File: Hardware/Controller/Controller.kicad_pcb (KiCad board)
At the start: 2 copper layers, 33 x 123.2 mm, 6 parts

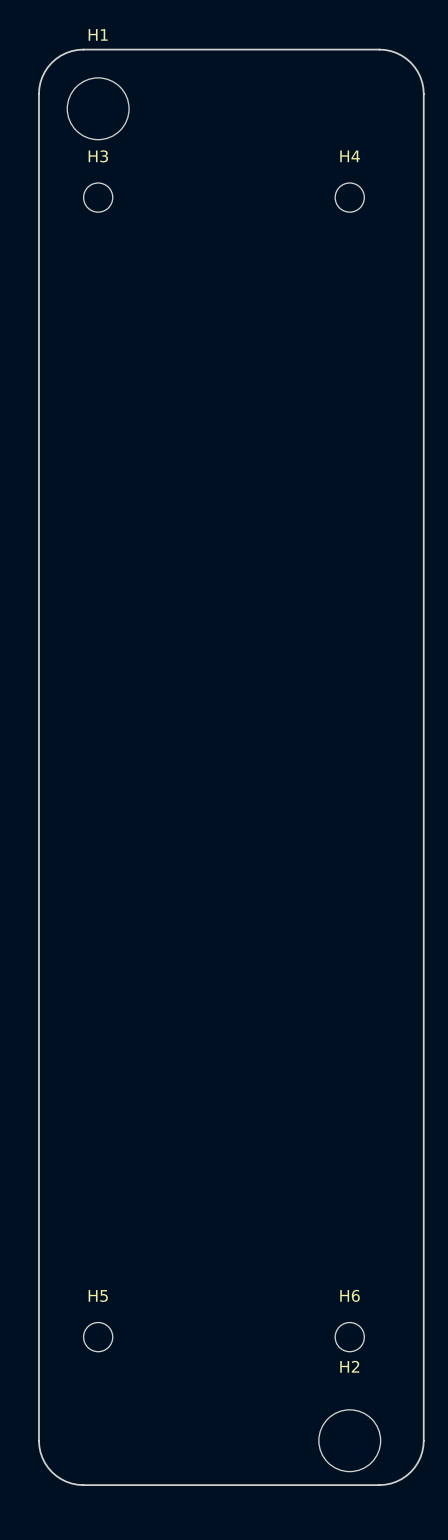
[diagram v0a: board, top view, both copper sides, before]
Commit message: Updated fitting for SP 2090 enclosure
Better fit, but still not perfect.
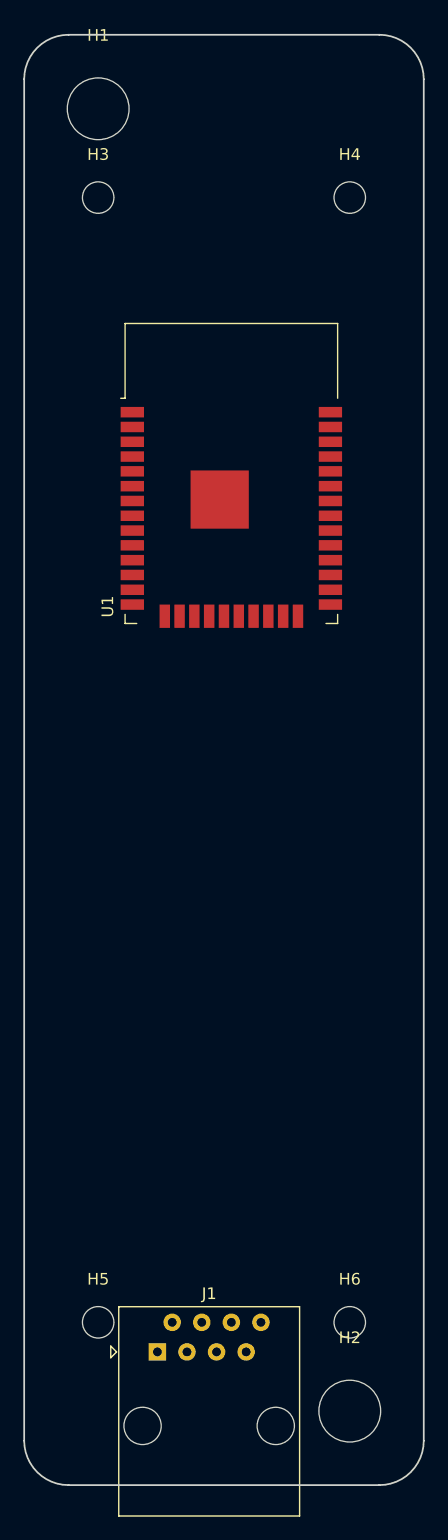
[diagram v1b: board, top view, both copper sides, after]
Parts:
- added J1: 8P8C, Connector_RJ:RJ45_Amphenol_54602-x08_Horizontal, F.Cu at (25.4, 127.0)
- added U1: ESP32-WROOM-32D, RF_Module:ESP32-WROOM-32, F.Cu at (31.8, 54.6)
- H3, H4, H5, H6: footprint MountingHole:MountingHole_2.5mm -> MountingHole:MountingHole_2.7mm_M2.5
- moved H2 2.54 mm to (41.9, 132.1)
- moved H5 1.27 mm to (20.3, 124.5)
- moved H6 1.27 mm to (41.9, 124.5)
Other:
- board size 33 x 123.2 mm -> 34.3 x 124.5 mm

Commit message: Finished case-specific layout parts
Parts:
- moved J1 109.8 mm to (133.5, 108.0)
- moved U1 107.9 mm to (136.8, 79.6)
- moved H3 0.80 mm to (20.8, 27.3)
- moved H4 0.70 mm to (42.2, 27.3)
- moved H5 0.54 mm to (20.8, 124.7)
- moved H1 0.48 mm to (20.8, 20.3)
- moved H2 0.48 mm to (42.2, 131.7)
- moved H6 0.38 mm to (42.2, 124.7)
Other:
- board size 34.3 x 124.5 mm -> 35 x 124 mm
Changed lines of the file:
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@@
   (general
     (thickness 1.6)
-    (drawings 10)
+    (drawings 9)
     (tracks 0)
     (zones 0)
@@
     (pad_to_mask_clearance 0.051)
     (solder_mask_min_width 0.25)
-    (aux_axis_origin 15.24 15.24)
+    (aux_axis_origin 13.97 13.97)
     (visible_elements 7FFFFFFF)
     (pcbplotparams
@@
   )
   (module MountingHole:MountingHole_5.3mm_M5 (layer F.Cu)
-    (at 20.32 20.32)
+    (at 20.8 20.3)
     (descr "Mounting Hole 5.3mm, no annular, M5")
     (tags "mounting hole 5.3mm no annular m5")
@@
   )
   (module MountingHole:MountingHole_5.3mm_M5 (layer F.Cu)
-    (at 41.91 132.08)
+    (at 42.2 131.7)
     (descr "Mounting Hole 5.3mm, no annular, M5")
     (tags "mounting hole 5.3mm no annular m5")
@@
   )
   (module RF_Module:ESP32-WROOM-32 (layer F.Cu)
-    (at 31.75 54.61)
+    (at 136.75 79.61)
     (descr "Single 2.4 GHz Wi-Fi and Bluetooth combo chip https://www.espressif.com/sites/default/files/documentation/esp32-wroom-32_datasheet_en.pdf")
     (tags "Single 2.4 GHz Wi-Fi and Bluetooth combo  chip")
@@
   )
   (module Connector_RJ:RJ45_Amphenol_54602-x08_Horizontal (layer F.Cu)
-    (at 25.4 127)
+    (at 133.5 108)
     (descr "8 Pol Shallow Latch Connector, Modjack, RJ45 (https://cdn.amphenol-icc.com/media/wysiwyg/files/drawing/c-bmj-0102.pdf)")
     (tags RJ45)
@@
   )
   (module MountingHole:MountingHole_2.7mm_M2.5 (layer F.Cu)
-    (at 20.32 27.94)
+    (at 20.8 27.3)
     (descr "Mounting Hole 2.7mm, no annular, M2.5")
     (tags "mounting hole 2.7mm no annular m2.5")
@@
   )
   (module MountingHole:MountingHole_2.7mm_M2.5 (layer F.Cu)
-    (at 41.91 27.94)
+    (at 42.2 27.3)
     (descr "Mounting Hole 2.7mm, no annular, M2.5")
     (tags "mounting hole 2.7mm no annular m2.5")
@@
   )
   (module MountingHole:MountingHole_2.7mm_M2.5 (layer F.Cu)
-    (at 20.32 124.46)
+    (at 20.8 124.7)
     (descr "Mounting Hole 2.7mm, no annular, M2.5")
     (tags "mounting hole 2.7mm no annular m2.5")
@@
   )
   (module MountingHole:MountingHole_2.7mm_M2.5 (layer F.Cu)
-    (at 41.91 124.46)
+    (at 42.2 124.7)
     (descr "Mounting Hole 2.7mm, no annular, M2.5")
     (tags "mounting hole 2.7mm no annular m2.5")
@@
     (pad 1 np_thru_hole circle (at 0 0) (size 2.7 2.7) (drill 2.7) (layers *.Cu *.Mask))
   )
-  (dimension 97.79 (width 0.3) (layer F.SilkS)
-    (gr_text "97,790 mm" (at 59.25 76.835 270) (layer F.SilkS)
-      (effects (font (size 1.5 1.5) (thickness 0.3)))
-    )
-    (feature1 (pts (xy 52.07 125.73) (xy 57.736421 125.73)))
-    (feature2 (pts (xy 52.07 27.94) (xy 57.736421 27.94)))
-    (crossbar (pts (xy 57.15 27.94) (xy 57.15 125.73)))
-    (arrow1a (pts (xy 57.15 125.73) (xy 56.563579 124.603496)))
-    (arrow1b (pts (xy 57.15 125.73) (xy 57.736421 124.603496)))
-    (arrow2a (pts (xy 57.15 27.94) (xy 56.563579 29.066504)))
-    (arrow2b (pts (xy 57.15 27.94) (xy 57.736421 29.066504)))
-  )
-  (target plus (at 15.24 15.24) (size 5) (width 0.15) (layer Edge.Cuts))
-  (gr_arc (start 17.78 134.62) (end 13.97 134.62) (angle -90) (layer Edge.Cuts) (width 0.15))
-  (gr_arc (start 44.45 134.62) (end 44.45 138.43) (angle -90) (layer Edge.Cuts) (width 0.15))
-  (gr_arc (start 17.78 17.78) (end 17.78 13.97) (angle -90) (layer Edge.Cuts) (width 0.15))
-  (gr_arc (start 44.45 17.78) (end 48.26 17.78) (angle -90) (layer Edge.Cuts) (width 0.15))
-  (gr_line (start 44.45 13.97) (end 17.78 13.97) (layer Edge.Cuts) (width 0.15))
-  (gr_line (start 48.26 134.62) (end 48.26 17.78) (layer Edge.Cuts) (width 0.15))
-  (gr_line (start 17.78 138.43) (end 44.45 138.43) (layer Edge.Cuts) (width 0.15))
-  (gr_line (start 13.97 17.78) (end 13.97 134.62) (layer Edge.Cuts) (width 0.15))
+  (gr_arc (start 19 133) (end 14 133) (angle -90) (layer Edge.Cuts) (width 0.15))
+  (gr_arc (start 44 133) (end 44 138) (angle -90) (layer Edge.Cuts) (width 0.15))
+  (gr_arc (start 44 19) (end 49 19) (angle -90) (layer Edge.Cuts) (width 0.15))
+  (gr_arc (start 19 19) (end 19 14) (angle -90) (layer Edge.Cuts) (width 0.15))
+  (gr_line (start 44 14) (end 19 14) (layer Edge.Cuts) (width 0.15))
+  (gr_line (start 49 133) (end 49 19) (layer Edge.Cuts) (width 0.15))
+  (gr_line (start 19 138) (end 44 138) (layer Edge.Cuts) (width 0.15))
+  (gr_line (start 14 19) (end 14 133) (layer Edge.Cuts) (width 0.15))
+  (target plus (at 31.5 76) (size 5) (width 0.15) (layer Edge.Cuts))
 )

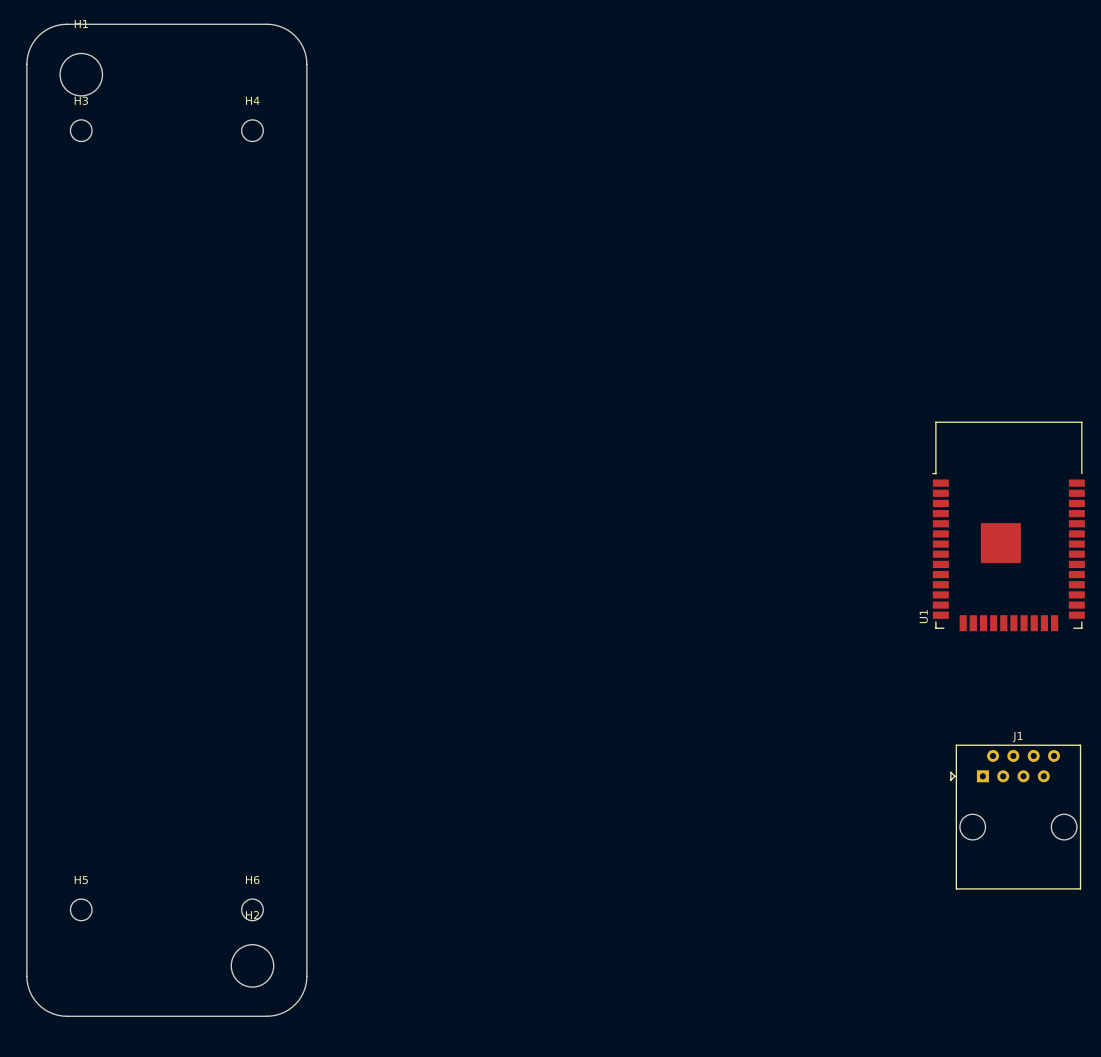
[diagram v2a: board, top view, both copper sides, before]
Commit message: Added a first set of parts
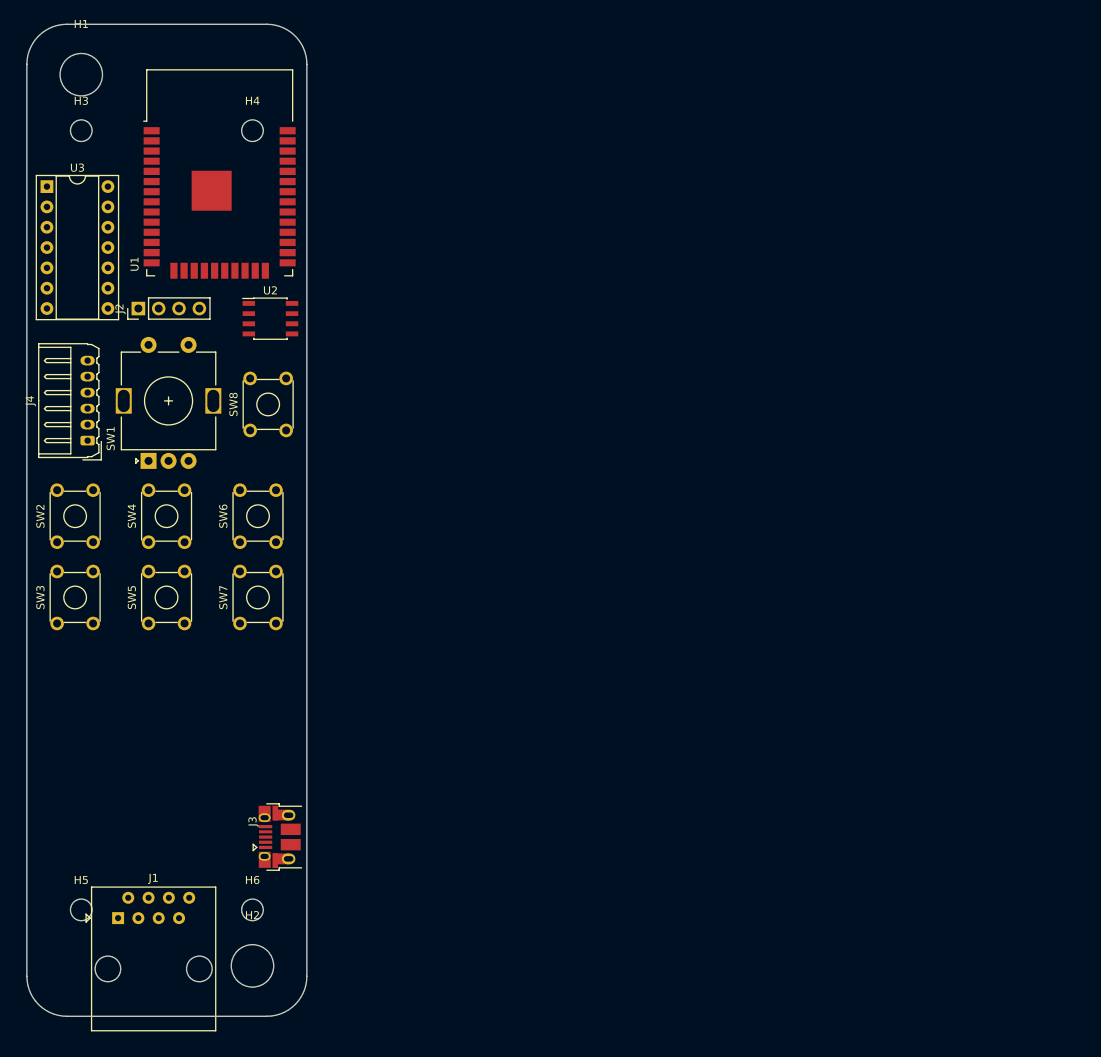
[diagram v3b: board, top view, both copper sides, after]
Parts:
- added J2: LCD Header, Connector_PinHeader_2.54mm:PinHeader_1x04_P2.54mm_Vertical, F.Cu at (27.9, 49.5)
- added J3: USB_B_Micro, Connector_USB:USB_Micro-B_Amphenol_10103594-0001LF_Horizontal, F.Cu at (45.6, 115.6)
- added J4: S88 ShiftRegister, Connector_Molex:Molex_Micro-Latch_53254-0670_1x06_P2.00mm_Horizontal, F.Cu at (21.6, 66.0)
- added SW1: Rotary_Encoder_Switch, Rotary_Encoder:RotaryEncoder_Alps_EC11E-Switch_Vertical_H20mm, F.Cu at (29.2, 68.6)
- added SW2: SW_Push_Dual, Button_Switch_THT:SW_TH_Tactile_Omron_B3F-10xx, F.Cu at (17.8, 78.7)
- added SW3: SW_Push_Dual, Button_Switch_THT:SW_TH_Tactile_Omron_B3F-10xx, F.Cu at (17.8, 88.9)
- added SW4: SW_Push_Dual, Button_Switch_THT:SW_TH_Tactile_Omron_B3F-10xx, F.Cu at (29.2, 78.7)
- added SW5: SW_Push_Dual, Button_Switch_THT:SW_TH_Tactile_Omron_B3F-10xx, F.Cu at (29.2, 88.9)
- added SW6: SW_Push_Dual, Button_Switch_THT:SW_TH_Tactile_Omron_B3F-10xx, F.Cu at (40.6, 78.7)
- added SW7: Shift, Button_Switch_THT:SW_TH_Tactile_Omron_B3F-10xx, F.Cu at (40.6, 88.9)
- added SW8: Stop, Button_Switch_THT:SW_TH_Tactile_Omron_B3F-10xx, F.Cu at (41.9, 64.8)
- added U2: TJA1051T, Package_SO:SOIC-8_3.9x4.9mm_P1.27mm, F.Cu at (44.5, 50.8)
- added U3: 74HC36, Package_DIP:DIP-14_W7.62mm_Socket, F.Cu at (16.5, 34.3)
- moved J1 109.5 mm to (25.4, 125.7)
- moved U1 108.0 mm to (38.1, 35.6)
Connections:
- H3 pad 1: (no net) -> GND
- H4 pad 1: (no net) -> GND
- H5 pad 1: (no net) -> GND
- H6 pad 1: (no net) -> GND
- U1 pad 1: Net-(U1-Pad1) -> GND
- U1 pad 15: Net-(U1-Pad1) -> GND
- U1 pad 38: Net-(U1-Pad1) -> GND

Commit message: Added more parts
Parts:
- added C1: 10n, Capacitor_SMD:C_0805_2012Metric_Pad1.15x1.40mm_HandSolder, B.Cu at (30.5, 66.0)
- added C10: 10n, Capacitor_SMD:C_0805_2012Metric_Pad1.15x1.40mm_HandSolder, B.Cu at (30.5, 57.1)
- added C2: 10n, Capacitor_SMD:C_0805_2012Metric_Pad1.15x1.40mm_HandSolder, B.Cu at (33.0, 66.0)
- added C3: 10n, Capacitor_SMD:C_0805_2012Metric_Pad1.15x1.40mm_HandSolder, B.Cu at (75.3, 90.2)
- added C4: 10n, Capacitor_SMD:C_0805_2012Metric_Pad1.15x1.40mm_HandSolder, B.Cu at (57.9, 56.3)
- added C5: 10n, Capacitor_SMD:C_0805_2012Metric_Pad1.15x1.40mm_HandSolder, B.Cu at (75.3, 85.6)
- added C6: 10n, Capacitor_SMD:C_0805_2012Metric_Pad1.15x1.40mm_HandSolder, B.Cu at (76.8, 90.2)
- added C7: 10n, Capacitor_SMD:C_0805_2012Metric_Pad1.15x1.40mm_HandSolder, B.Cu at (39.0, 91.5)
- added C8: 10n, Capacitor_SMD:C_0805_2012Metric_Pad1.15x1.40mm_HandSolder, B.Cu at (42.0, 85.0)
- added C9: 10n, Capacitor_SMD:C_0805_2012Metric_Pad1.15x1.40mm_HandSolder, B.Cu at (76.8, 85.6)
- added R1: 10k, Resistor_SMD:R_0603_1608Metric_Pad1.05x0.95mm_HandSolder, B.Cu at (27.9, 64.1)
- added R10: 10k, Resistor_SMD:R_0603_1608Metric_Pad1.05x0.95mm_HandSolder, B.Cu at (78.2, 82.3)
- added R11: 10k, Resistor_SMD:R_0603_1608Metric_Pad1.05x0.95mm_HandSolder, B.Cu at (79.7, 85.6)
- added R12: 10k, Resistor_SMD:R_0603_1608Metric_Pad1.05x0.95mm_HandSolder, B.Cu at (76.8, 74.5)
- added R13: 10k, Resistor_SMD:R_0603_1608Metric_Pad1.05x0.95mm_HandSolder, B.Cu at (76.8, 69.9)
- added R14: 10k, Resistor_SMD:R_0603_1608Metric_Pad1.05x0.95mm_HandSolder, B.Cu at (74.9, 79.0)
- added R15: 10k, Resistor_SMD:R_0603_1608Metric_Pad1.05x0.95mm_HandSolder, B.Cu at (83.8, 82.3)
- added R16: 10k, Resistor_SMD:R_0603_1608Metric_Pad1.05x0.95mm_HandSolder, B.Cu at (78.2, 74.5)
- added R17: 10k, Resistor_SMD:R_0603_1608Metric_Pad1.05x0.95mm_HandSolder, B.Cu at (78.2, 69.9)
- added R18: 10k, Resistor_SMD:R_0603_1608Metric_Pad1.05x0.95mm_HandSolder, B.Cu at (79.7, 79.0)
- added R19: 10k, Resistor_SMD:R_0603_1608Metric_Pad1.05x0.95mm_HandSolder, B.Cu at (34.3, 58.4)
- added R2: 10k, Resistor_SMD:R_0603_1608Metric_Pad1.05x0.95mm_HandSolder, B.Cu at (28.3, 66.0)
- added R20: 10k, Resistor_SMD:R_0603_1608Metric_Pad1.05x0.95mm_HandSolder, B.Cu at (34.3, 57.1)
- added R3: 10k, Resistor_SMD:R_0603_1608Metric_Pad1.05x0.95mm_HandSolder, B.Cu at (34.3, 63.8)
- added R4: 10k, Resistor_SMD:R_0603_1608Metric_Pad1.05x0.95mm_HandSolder, B.Cu at (35.6, 66.0)
- added R5: 10k, Resistor_SMD:R_0603_1608Metric_Pad1.05x0.95mm_HandSolder, B.Cu at (20.0, 83.5)
- added R6: 10k, Resistor_SMD:R_0603_1608Metric_Pad1.05x0.95mm_HandSolder, B.Cu at (75.3, 74.5)
- added R7: 10k, Resistor_SMD:R_0603_1608Metric_Pad1.05x0.95mm_HandSolder, B.Cu at (18.7, 86.4)
- added R8: 10k, Resistor_SMD:R_0603_1608Metric_Pad1.05x0.95mm_HandSolder, F.Cu at (25.4, 92.7)
- added R9: 10k, Resistor_SMD:R_0603_1608Metric_Pad1.05x0.95mm_HandSolder, B.Cu at (23.0, 84.5)
- added U4: CH340C, Package_SO:SOIC-16_3.9x9.9mm_P1.27mm, F.Cu at (44.5, 104.1)
- U1: value ESP32-WROOM-32D -> ESP32-WROOM-32
- U2: moved to B.Cu
- U3: value 74HC36 -> 74LS367; footprint Package_DIP:DIP-14_W7.62mm_Socket -> Package_SO:SOP-16_4.4x10.4mm_P1.27mm
- moved U2 11.8 mm to (39.8, 39.9), turned to 180 degrees
- moved J4 7.56 mm to (21.0, 58.5)
- moved U3 5.47 mm to (20.0, 38.5), turned to 180 degrees
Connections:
- J1 pad 1: (no net) -> Net-(J1-Pad1)
- J1 pad 2: (no net) -> Net-(J1-Pad2)
- J1 pad 3: (no net) -> Net-(J1-Pad3)
- J1 pad 4: (no net) -> Net-(J1-Pad4)
- J1 pad 5: (no net) -> GND
- J1 pad 6: (no net) -> GND
- J1 pad 7: (no net) -> Net-(J1-Pad7)
- J1 pad 8: (no net) -> Net-(J1-Pad8)
- J2 pad 1: (no net) -> GND
- J2 pad 2: (no net) -> VCC
- J2 pad 3: (no net) -> /I2C_SCL
- J2 pad 4: (no net) -> /I2C_SDA
- J3 pad 1: (no net) -> Net-(J3-Pad1)
- J3 pad 2: (no net) -> Net-(J3-Pad2)
- J3 pad 3: (no net) -> Net-(J3-Pad3)
- J3 pad 4: (no net) -> Net-(J3-Pad4)
- J4 pad 1: (no net) -> /S88_DATA
- J4 pad 2: (no net) -> GND
- J4 pad 3: (no net) -> Net-(J4-Pad3)
- J4 pad 4: (no net) -> Net-(J4-Pad4)
- J4 pad 5: (no net) -> Net-(J4-Pad5)
- J4 pad 6: (no net) -> VCC
- SW1 pad A: (no net) -> Net-(R1-Pad1)
- SW1 pad B: (no net) -> Net-(R3-Pad1)
- SW1 pad S1: (no net) -> Net-(R19-Pad2)
- U1 pad 10: (no net) -> Net-(U1-Pad10)
- U1 pad 11: (no net) -> /I2C_SCL
- U1 pad 12: (no net) -> /I2C_SDA
- U1 pad 13: (no net) -> Net-(C5-Pad2)
- U1 pad 14: (no net) -> Net-(C3-Pad2)
- U1 pad 16: (no net) -> Net-(C4-Pad2)
- U1 pad 17: (no net) -> Net-(U1-Pad17)
- U1 pad 18: (no net) -> Net-(U1-Pad18)
- U1 pad 19: (no net) -> Net-(U1-Pad19)
- U1 pad 2: (no net) -> VCC
- U1 pad 20: (no net) -> Net-(U1-Pad20)
- U1 pad 21: (no net) -> Net-(U1-Pad21)
- U1 pad 22: (no net) -> Net-(U1-Pad22)
- U1 pad 23: (no net) -> Net-(C6-Pad2)
- U1 pad 24: (no net) -> Net-(U1-Pad24)
- U1 pad 25: (no net) -> Net-(U1-Pad25)
- U1 pad 26: (no net) -> Net-(U1-Pad26)
- U1 pad 27: (no net) -> Net-(C7-Pad2)
- U1 pad 28: (no net) -> Net-(C8-Pad2)
- U1 pad 29: (no net) -> Net-(U1-Pad29)
- U1 pad 3: (no net) -> Net-(U1-Pad3)
- U1 pad 30: (no net) -> Net-(U1-Pad30)
- U1 pad 31: (no net) -> Net-(C9-Pad2)
- U1 pad 32: (no net) -> Net-(U1-Pad32)
- U1 pad 33: (no net) -> Net-(U1-Pad33)
- U1 pad 34: (no net) -> Net-(U1-Pad34)
- U1 pad 35: (no net) -> Net-(U1-Pad35)
- U1 pad 36: (no net) -> Net-(U1-Pad36)
- U1 pad 37: (no net) -> Net-(U1-Pad37)
- U1 pad 4: (no net) -> Net-(U1-Pad4)
- U1 pad 5: (no net) -> Net-(U1-Pad5)
- U1 pad 6: (no net) -> /S88_CLOCK_UC
- U1 pad 7: (no net) -> /S88_PS_UC
- U1 pad 8: (no net) -> /S88_RESET_UC
- U1 pad 9: (no net) -> /S88_DATA
- U2 pad 1: (no net) -> Net-(U1-Pad29)
- U2 pad 2: (no net) -> GND
- U2 pad 3: (no net) -> VCC
- U2 pad 4: (no net) -> Net-(U1-Pad26)
- U2 pad 5: (no net) -> Net-(U2-Pad5)
- U2 pad 6: (no net) -> Net-(J1-Pad2)
- U2 pad 7: (no net) -> Net-(J1-Pad1)
- U2 pad 8: (no net) -> Net-(U2-Pad8)
- U3 pad 1: (no net) -> GND
- U3 pad 10: (no net) -> GND
- U3 pad 11: (no net) -> Net-(U3-Pad11)
- U3 pad 12: (no net) -> GND
- U3 pad 13: (no net) -> Net-(U3-Pad13)
- U3 pad 14: (no net) -> GND
- U3 pad 2: (no net) -> /S88_RESET_UC
- U3 pad 3: (no net) -> Net-(J4-Pad5)
- U3 pad 4: (no net) -> /S88_PS_UC
- U3 pad 5: (no net) -> Net-(J4-Pad4)
- U3 pad 6: (no net) -> /S88_CLOCK_UC
- U3 pad 7: (no net) -> Net-(J4-Pad3)
- U3 pad 8: (no net) -> GND
- U3 pad 9: (no net) -> Net-(U3-Pad9)
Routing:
- net Net-(J1-Pad2): track 0.00 -> 106.6 mm
- net Net-(J1-Pad1): track 0.00 -> 100.9 mm
- net Net-(U1-Pad3): track 0.00 -> 86.7 mm
- net VCC: track 0.00 -> 66.6 mm, vias 0 -> 3
- net Net-(U1-Pad25): track 0.00 -> 56.6 mm, vias 0 -> 1
- net /S88_DATA: track 0.00 -> 25.5 mm
- net Net-(J4-Pad3): track 0.00 -> 22.5 mm
- net Net-(J4-Pad4): track 0.00 -> 17.7 mm
- net Net-(J3-Pad2): track 0.00 -> 15.4 mm, vias 0 -> 2
- net Net-(J3-Pad3): track 0.00 -> 13.5 mm
- net Net-(J4-Pad5): track 0.00 -> 12.8 mm
- net /I2C_SCL: track 0.00 -> 12.8 mm
- net /I2C_SDA: track 0.00 -> 11.7 mm
- net /S88_RESET_UC: track 0.00 -> 9.41 mm
- net /S88_PS_UC: track 0.00 -> 8.20 mm
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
